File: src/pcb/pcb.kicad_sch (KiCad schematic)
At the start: 8 parts, among them U1 LM317_TO-220

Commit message: Add: PCB layout
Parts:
- added J1, J2: Conn_01x02, TerminalBlock:TerminalBlock_bornier-2_P5.08mm, symbol Connector_Generic:Conn_01x02
- C1: footprint (none) -> Capacitor_THT:C_Disc_D5.0mm_W2.5mm_P5.00mm
- C2, C3: footprint (none) -> Capacitor_THT:C_Radial_D4.0mm_H7.0mm_P1.50mm
- R1: footprint (none) -> Resistor_THT:R_Axial_DIN0207_L6.3mm_D2.5mm_P10.16mm_Horizontal
- RV1: footprint (none) -> Potentiometer_THT:Potentiometer_Alps_RK163_Single_Horizontal
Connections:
- net +12V: now also J1.1 (Pin_1)
- net GND: now also J1.2 (Pin_2), J2.2 (Pin_2)
- net Vout: now reaches C3.1, D1.2 (A), D2.1 (K), R1.1, U1.2 (VO)
- net Vout: now also J2.1 (Pin_1)
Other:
- moved on the sheet: C1, C2, C3, D1, D2, R1, RV1, U1

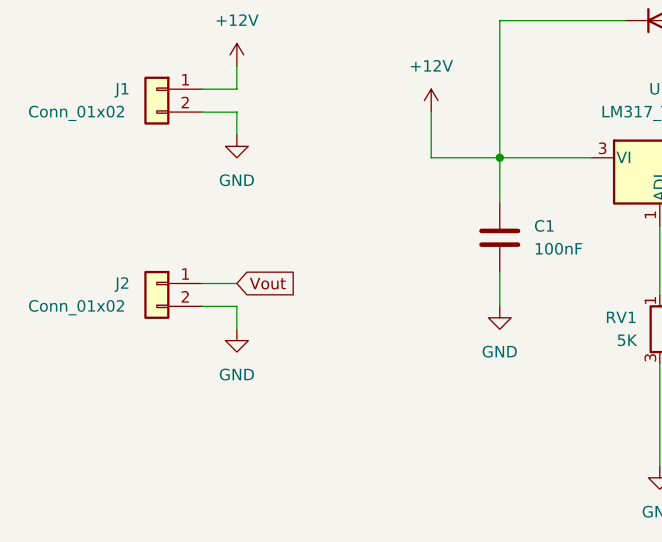
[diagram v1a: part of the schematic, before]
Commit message: Fix: Remove island
Add: Terminal Block STEP
Add: Potentiometer STEP
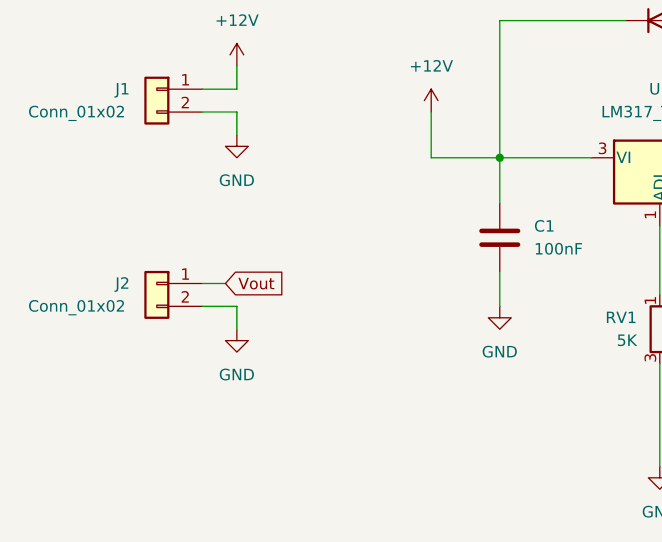
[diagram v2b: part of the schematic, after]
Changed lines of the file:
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@@
-    (stroke (width 0) (type default) (color 0 0 0 0))
-  )
-  (wire (pts (xy 52.07 92.71) (xy 55.88 92.71))
     (stroke (width 0) (type default) (color 0 0 0 0))
   )
@@
   )
   (wire (pts (xy 85.09 76.2) (xy 95.25 76.2))
-    (stroke (width 0) (type default) (color 0 0 0 0))
-  )
-  (wire (pts (xy 52.07 90.17) (xy 55.88 90.17))
     (stroke (width 0) (type default) (color 0 0 0 0))
   )
@@
     (stroke (width 0) (type default) (color 0 0 0 0))
   )
+  (wire (pts (xy 52.07 92.71) (xy 55.88 92.71))
+    (stroke (width 0) (type default) (color 0 0 0 0))
+  )
   (wire (pts (xy 151.13 81.28) (xy 151.13 76.2))
     (stroke (width 0) (type default) (color 0 0 0 0))
@@
   )
   (wire (pts (xy 120.65 88.9) (xy 120.65 95.25))
+    (stroke (width 0) (type default) (color 0 0 0 0))
+  )
+  (wire (pts (xy 52.07 90.17) (xy 54.61 90.17))
     (stroke (width 0) (type default) (color 0 0 0 0))
   )
@@
     )
   )
-  (global_label "Vout" (shape input) (at 55.88 90.17 0) (fields_autoplaced)
+  (global_label "Vout" (shape input) (at 54.61 90.17 0) (fields_autoplaced)
     (effects (font (size 1.27 1.27)) (justify left))
-    (property "Intersheet References" "${INTERSHEET_REFS}" (id 0) (at 62.4055 90.0906 0)
+    (property "Intersheet References" "${INTERSHEET_REFS}" (id 0) (at 61.1355 90.0906 0)
       (effects (font (size 1.27 1.27)) (justify left) hide)
     )
